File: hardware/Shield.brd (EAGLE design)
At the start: 53.3 x 55.9 mm, 25 parts, among them J1 AVR_SPI_PRG_6PTH, Q8 TIP120, U2 LM78XX-TO252-3, U4 ATMEGA328P_PDIP, Y1 16Mhz

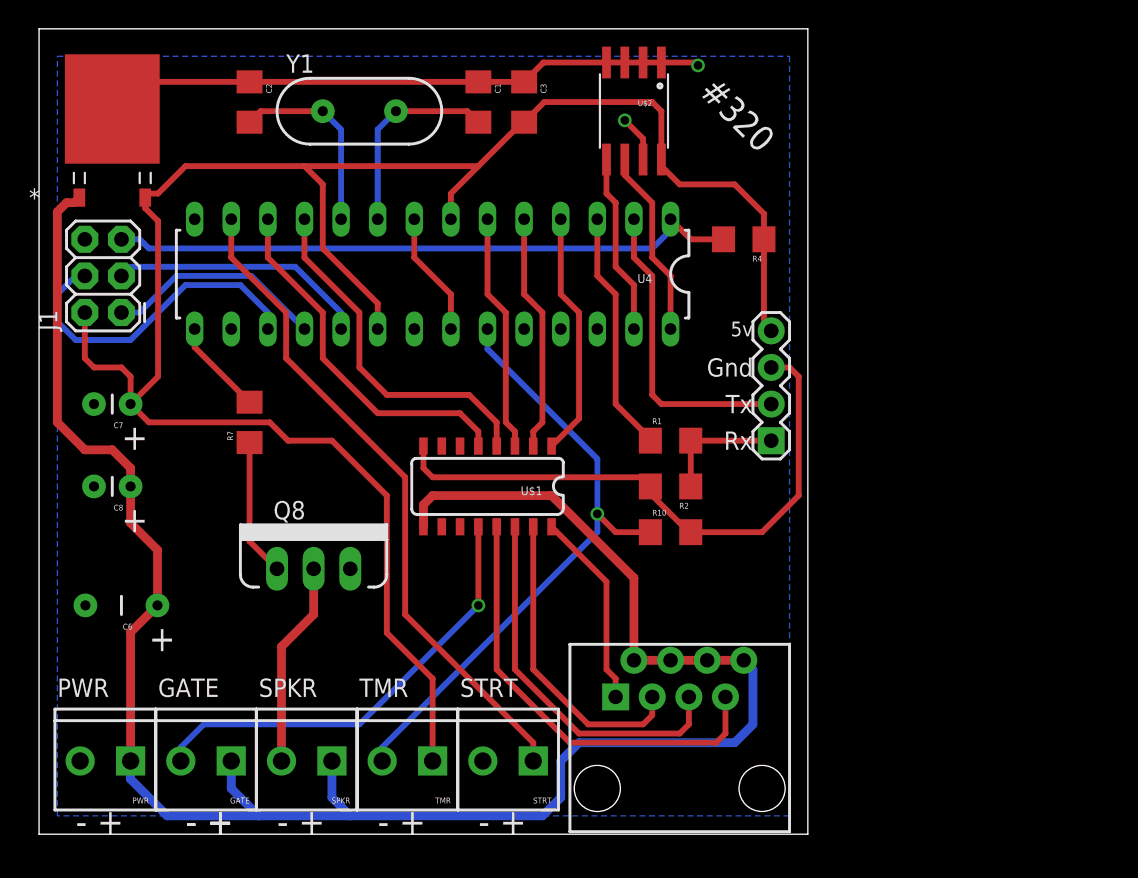
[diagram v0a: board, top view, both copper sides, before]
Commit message: Restored lost RAM board design during migration from svn
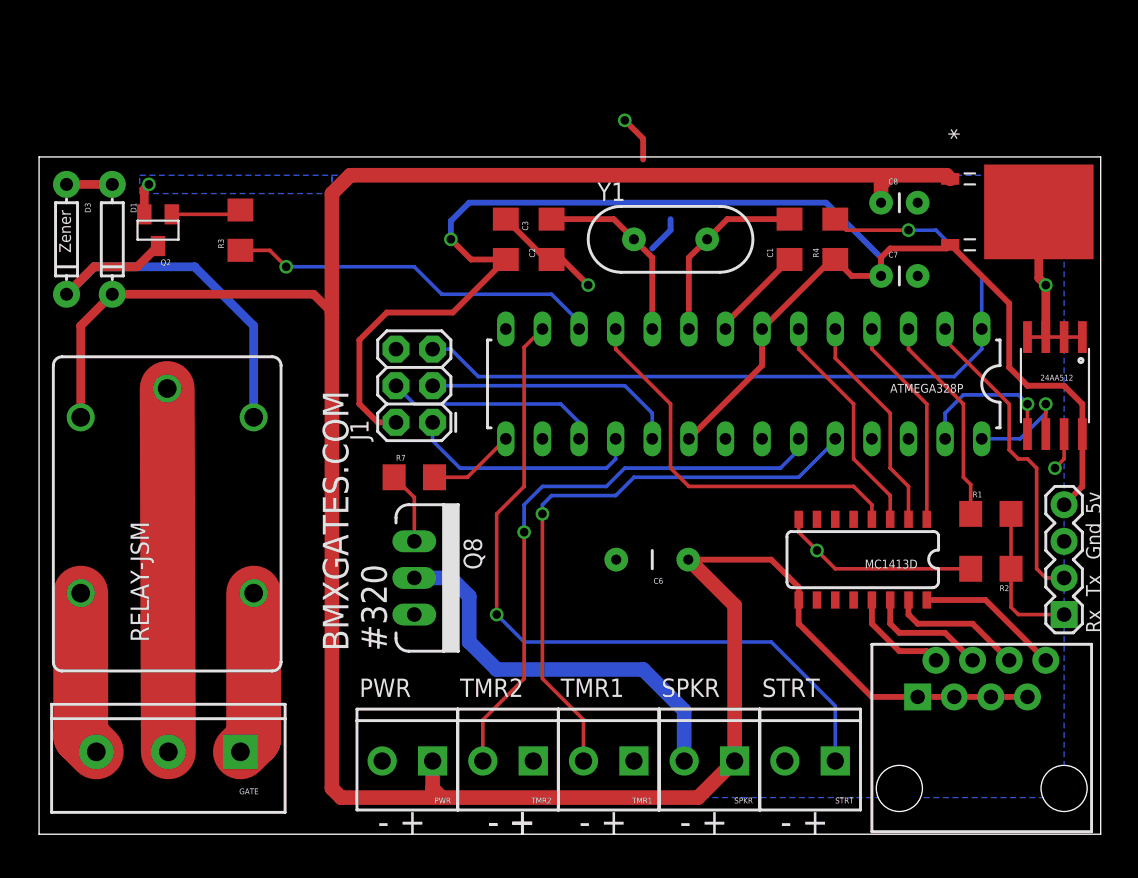
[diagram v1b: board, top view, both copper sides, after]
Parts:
- removed R10: 10K, SparkFun-Passives:1206
- removed TMR: (no value), SparkFun-Connectors:SCREWTERMINAL-3.5MM-2
- removed U$1: MC1413D, ucigate:SO016
- removed U$2: 24AAXXX, ucigate:SOIC-8-EIAJ
- removed U2: LM78XX-TO252-3, element14-com:TO252-3
- removed U4: ATMEGA328P_PDIP, SparkFun-DigitalIC:DIL28-3
- added 24AA512: 24AAXXX, ucigate:SOIC-8-EIAJ
- added ATMEGA328P: ATMEGA328P_PDIP, SparkFun-DigitalIC:DIL28-3
- added D1: (no value), SparkFun-DiscreteSemi:DIODE-1N4148
- added D3: Zener, SparkFun-DiscreteSemi:DIODE-1N4148-KIT
- added LM78M05: LM78XX-TO252-3, element14-com:TO252-3
- added MC1413D: MC1413D, ucigate:SO016
- added Q2: MMBT5088, SparkFun-DiscreteSemi:SOT23
- added R3: 1K, SparkFun-Passives:1206
- added RELAY-JSM: RELAY-JSMJSM, petrocik:JS-M
- added TMR1, TMR2: (no value), SparkFun-Connectors:SCREWTERMINAL-3.5MM-2
- GATE: device SparkFun-Connectors:SCREWTERMINAL-3.5MM-2 -> SparkFun-Connectors:SCREWTERMINAL-5MM-3
- moved C8 55.7 mm to (58.4, 43.8), turned to 0 degrees
- moved C7 52.8 mm to (58.4, 38.7), turned to 0 degrees
- moved C6 37.0 mm to (42.5, 19.1)
- moved SPKR 27.9 mm to (48.3, 5.08)
- moved BT_HDR 23.6 mm to (71.1, 15.2)
- moved C1 23.6 mm to (52.1, 41.3), turned to 90 degrees
- moved Y1 23.3 mm to (43.8, 41.3)
- moved C2 23.0 mm to (35.6, 41.3), turned to 90 degrees
- moved R2 22.9 mm to (66.0, 18.4)
- moved J1 22.9 mm to (27.3, 28.6)
- moved R1 22.8 mm to (66.0, 22.2)
- moved LIGHT 21.0 mm to (65.4, 3.17)
- moved PWR 21.0 mm to (27.3, 5.08)
- moved STRT 21.0 mm to (55.2, 5.08)
- moved R7 12.0 mm to (26.0, 24.8), turned to 0 degrees
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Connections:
- removed net GATE: GATE.2, U$1.12
- new net A1: ATMEGA328P.24, TMR1.2
- new net COIL: D3.C, Q2.3, RELAY-JSM.2
- new net DIODENODE: D1.A, D3.A
- new net N$6: GATE.2, RELAY-JSM.C
- new net N$9: Q2.1, R3.2
- new net NC: GATE.1, RELAY-JSM.NC
- new net NO: GATE.3, RELAY-JSM.NO
- net 5V: now also 24AA512.8, ATMEGA328P.20, ATMEGA328P.7, LM78M05.3; no longer TMR.1, U$2.8, U2.3, U4.20, U4.7
- net A0: now also ATMEGA328P.23, TMR2.2; no longer R10.1, TMR.2, U4.23
- net A4: now also 24AA512.5, ATMEGA328P.27; no longer U$2.5, U4.27
- net A5: now also 24AA512.6, ATMEGA328P.28; no longer U$2.6, U4.28
- net D2: now also ATMEGA328P.4, MC1413D.1; no longer U$1.1, U4.4
- net D3: now also ATMEGA328P.5, MC1413D.2; no longer U$1.2, U4.5
- net D4: now also ATMEGA328P.6, MC1413D.3; no longer U$1.3, U4.6
- net D5: now also ATMEGA328P.11, MC1413D.4; no longer U$1.4, U4.11
- net D6: now also ATMEGA328P.12, R3.1; no longer U$1.5, U4.12
- net D7: now also ATMEGA328P.13; no longer U4.13
- net D9: now also ATMEGA328P.15; no longer U4.15
- net GND: now also 24AA512.1, 24AA512.2, 24AA512.3, 24AA512.4, 24AA512.7, ATMEGA328P.22, ATMEGA328P.8, LM78M05.2, MC1413D.8, Q2.2, TMR1.1, TMR2.1; no longer R10.2, U$1.8, U$2.1, U$2.2, U$2.3, U$2.4, U$2.7, U2.2, U4.22, U4.8
- net MISO: now also ATMEGA328P.18; no longer U4.18
- net MOSI: now also ATMEGA328P.17; no longer U4.17
- net N$15: now also ATMEGA328P.9; no longer U4.9
- net N$2: now also LIGHT.8, MC1413D.16; no longer LIGHT.1, U$1.16
- net N$24: now also ATMEGA328P.10; no longer U4.10
- net N$3: now also LIGHT.4, MC1413D.14; no longer LIGHT.3, U$1.15
- net N$4: now also LIGHT.2, MC1413D.13; no longer LIGHT.5, U$1.14
- net N$5: now also LIGHT.6, MC1413D.15; no longer LIGHT.7, U$1.13
- net RESET: now also ATMEGA328P.1; no longer U4.1
- net RX: now also ATMEGA328P.2; no longer U4.2
- net SCK: now also ATMEGA328P.19; no longer U4.19
- net TX: now also ATMEGA328P.3; no longer U4.3
- net VCC: now also D1.C, LIGHT.1, LIGHT.3, LIGHT.5, LIGHT.7, LM78M05.1, MC1413D.9, RELAY-JSM.1; no longer GATE.1, LIGHT.2, LIGHT.4, LIGHT.6, LIGHT.8, U$1.9, U2.1
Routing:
- net VCC: track 140.2 -> 188.6 mm
- net GND: track 96.3 -> 48.9 mm, vias 2 -> 6
- net A1: track 0.00 -> 41.2 mm, vias 0 -> 1
- net 5V: track 141.7 -> 109.0 mm, vias 0 -> 1
- net GATE: track 31.1 -> 0.00 mm, vias 1 -> 0
- net COIL: track 0.00 -> 29.8 mm
- net N$6: track 0.00 -> 25.2 mm
- net N$5: track 30.7 -> 9.31 mm
- net N$4: track 26.0 -> 7.14 mm
- net RESET: track 44.4 -> 59.3 mm, vias 0 -> 1
- net N$12: track 14.3 -> 27.9 mm
- net N$3: track 21.3 -> 8.41 mm
- net NO: track 0.00 -> 11.5 mm
- net NC: track 0.00 -> 11.4 mm
- net MOSI: track 23.0 -> 14.9 mm
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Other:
- board size 53.3 x 55.9 mm -> 73.7 x 47 mm
- board text added: "BMXGATES.COM #320"
- board text added: "ISP"
- board text added: "Ram Gate v3.1"
- board text added: "TMR1"
- board text added: "TMR2"
- board text removed: "#320"
- board text removed: "+"
- board text removed: "GATE"
- board text removed: "TMR"
- board text removed: "UCI Gate v3.0.1"

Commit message: Fixed rogue wires
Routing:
- net GND: track 48.9 -> 45.7 mm, vias 6 -> 5
- net RESET: track 59.3 -> 56.7 mm
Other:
- board text added: "UCI Gate v4.0-RAM"
- board text removed: "Ram Gate v3.1"
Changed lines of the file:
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@@
 <wire x1="73.66" y1="46.99" x2="0" y2="46.99" width="0" layer="20"/>
 <wire x1="0" y1="46.99" x2="0" y2="0" width="0" layer="20"/>
-<text x="22.86" y="43.815" size="1.778" layer="22" rot="MR0">Ram Gate v3.1</text>
+<text x="22.86" y="43.815" size="1.778" layer="22" rot="MR0">UCI Gate v4.0-RAM</text>
 <text x="51.435" y="0" size="1.778" layer="21">- +</text>
 <text x="44.45" y="0" size="1.778" layer="21">- +</text>
@@
 <via x="7.62" y="45.085" extent="1-16" drill="0.6" shape="square"/>
 <wire x1="7.305" y1="43.01" x2="7.305" y2="44.77" width="0.6096" layer="1"/>
-<wire x1="41.91" y1="46.8122" x2="41.91" y2="48.26" width="0.4064" layer="1"/>
-<wire x1="41.91" y1="48.26" x2="40.64" y2="49.53" width="0.4064" layer="1"/>
-<via x="40.64" y="49.53" extent="1-16" drill="0.6"/>
 </signal>
 <signal name="VCC">
@@
 <wire x1="60.325" y1="41.91" x2="56.01" y2="41.91" width="0.254" layer="1"/>
 <wire x1="56.01" y1="41.91" x2="55.245" y2="42.675" width="0.254" layer="1"/>
-<wire x1="42.545" y1="40.64" x2="43.815" y2="41.91" width="0.4064" layer="16"/>
-<wire x1="43.815" y1="41.91" x2="43.815" y2="42.672" width="0.4064" layer="16"/>
 </signal>
 <signal name="D6">

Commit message: 4.2
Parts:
- removed TMR1, TMR2: (no value), SparkFun-Connectors:SCREWTERMINAL-3.5MM-2
- added JP3: TMR, SparkFun-Connectors:SCREWTERMINAL-3.5MM-4
- added PMR2: TMR, SparkFun-Connectors:SCREWTERMINAL-3.5MM-2
- added R10: 10K, petrocik:SO016
- moved PWR 37.5 mm to (20.3, 41.9), turned to 0 degrees
- moved C6 3.18 mm to (44.5, 16.5), turned to 90 degrees
- moved Q8 1.91 mm to (24.1, 17.8)
- moved Q2 1.27 mm to (9.53, 41.9)
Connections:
- new net A2: ATMEGA328P.25, R10.11, R10.12
- new net A3: ATMEGA328P.26, R10.10, R10.9
- new net N$11: JP3.4, R10.7
- new net N$18: JP3.2, R10.3
- new net N$20: JP3.3, R10.5
- new net N$7: JP3.1, R10.1
- net A0: now also R10.15, R10.16; no longer TMR2.2
- net A1: now also R10.13, R10.14; no longer TMR1.2
- net GND: now also PMR2.2, R10.2, R10.4, R10.6, R10.8; no longer TMR1.1, TMR2.1
- net VCC: now also PMR2.1
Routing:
- net A3: track 0.00 -> 33.0 mm, vias 0 -> 1
- net GND: track 45.7 -> 78.2 mm
- net A2: track 0.00 -> 29.1 mm, vias 0 -> 1
- net N$7: track 0.00 -> 25.3 mm
- net N$18: track 0.00 -> 20.2 mm
- net A0: track 40.4 -> 21.3 mm
- net A1: track 41.2 -> 25.5 mm
- net N$20: track 0.00 -> 14.4 mm
- net N$11: track 0.00 -> 11.3 mm
- net D7: track 51.1 -> 42.5 mm
- net VCC: track 188.6 -> 185.1 mm
- net N$12: track 27.9 -> 29.8 mm
- net N$9: track 4.89 -> 3.62 mm
- net COIL: track 29.8 -> 30.8 mm
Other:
- board text added: "------TIMERS------"
- board text added: "1 2 3 4"
- board text added: "UCI Gate v4.2-RAM"
- board text removed: "TMR1"
- board text removed: "TMR2"
- board text removed: "UCI Gate v4.0-RAM"

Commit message: Starting 4.3 board developement
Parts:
- removed D1: (no value), SparkFun-DiscreteSemi:DIODE-1N4148
- removed D3: Zener, SparkFun-DiscreteSemi:DIODE-1N4148-KIT
- removed GATE: (no value), SparkFun-Connectors:SCREWTERMINAL-5MM-3
- removed JP3: TMR, SparkFun-Connectors:SCREWTERMINAL-3.5MM-4
- removed Q2: MMBT5088, SparkFun-DiscreteSemi:SOT23
- removed R3: 1K, SparkFun-Passives:1206
- removed RELAY-JSM: RELAY-JSMJSM, petrocik:JS-M
- added J2: TMR, SparkFun-Connectors:SCREWTERMINAL-3.5MM-4
- added J3: RELAY, SparkFun-Connectors:SCREWTERMINAL-3.5MM-3
- BT_HDR: device SparkFun-Connectors:1X04 -> SparkFun-Connectors:1X04@1
- moved Q8 5.08 mm to (29.2, 17.8)
- moved R10 3.81 mm to (36.8, 17.8)
- moved PMR2 1.27 mm to (27.3, 5.08)
- turned C3 to 90 degrees
- turned R4 to 270 degrees
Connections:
- removed net COIL: D3.C, Q2.3, RELAY-JSM.2
- removed net DIODENODE: D1.A, D3.A
- removed net N$6: GATE.2, RELAY-JSM.C
- removed net N$9: Q2.1, R3.2
- removed net NC: GATE.1, RELAY-JSM.NC
- removed net NO: GATE.3, RELAY-JSM.NO
- net 5V: now also J3.1
- net D6: now also J3.3; no longer R3.1
- net GND: now also J3.2; no longer Q2.2
- net N$11: now also J2.4; no longer JP3.4
- net N$18: now also J2.2; no longer JP3.2
- net N$20: now also J2.3; no longer JP3.3
- net N$7: now also J2.1; no longer JP3.1
- net VCC: no longer D1.C, RELAY-JSM.1
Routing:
- net COIL: track 30.8 -> 0.00 mm
- net N$6: track 25.2 -> 0.00 mm
- net GND: track 78.2 -> 60.9 mm, vias 5 -> 4
- net VCC: track 185.1 -> 170.5 mm
- net 5V: track 109.0 -> 121.9 mm, vias 1 -> 0
- net NO: track 11.5 -> 0.00 mm
- net NC: track 11.4 -> 0.00 mm
- net D6: track 26.1 -> 31.3 mm, vias 1 -> 0
- net N$12: track 29.8 -> 25.1 mm
- net N$7: track 25.3 -> 21.4 mm
- net N$9: track 3.62 -> 0.00 mm
- net N$18: track 20.2 -> 16.7 mm
- net DIODENODE: track 3.17 -> 0.00 mm
- net A0: track 21.3 -> 18.2 mm
- net A1: track 25.5 -> 22.4 mm
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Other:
- board size 73.7 x 47 mm -> 55.9 x 47 mm
- board text added: "+ IN -"
- board text added: "BMXGATES #320"
- board text added: "UCI Gate v4.3-RAM"
- board text removed: "BMXGATES.COM #320"
- board text removed: "UCI Gate v4.2-RAM"
